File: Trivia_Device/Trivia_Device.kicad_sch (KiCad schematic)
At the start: 5 parts, among them J1 Conn_01x16, J2 Conn_01x16, J3 Conn_01x16, J4 Conn_01x16, U1 BC40C

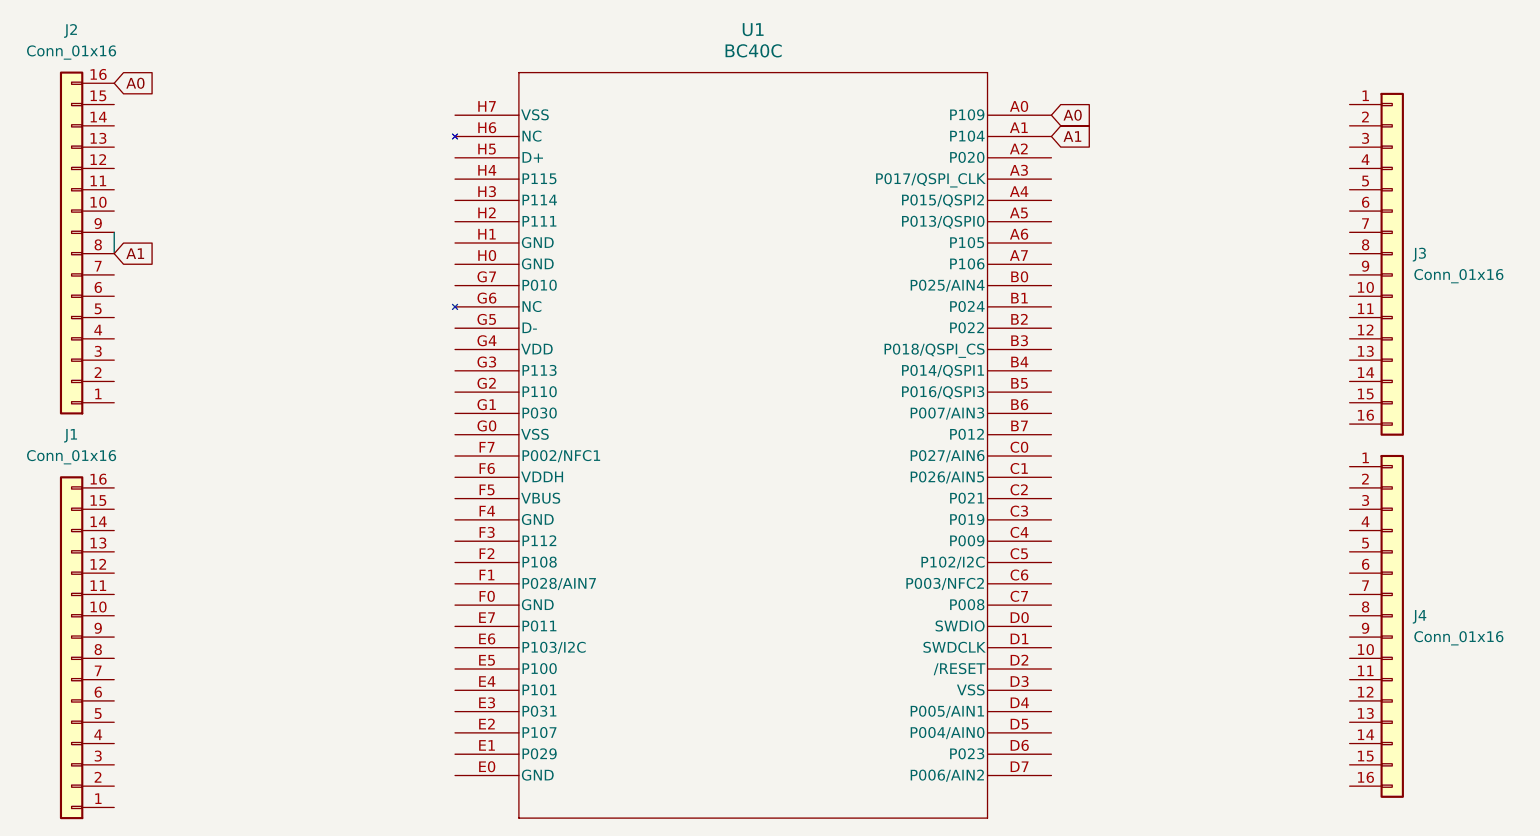
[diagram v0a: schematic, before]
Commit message: working on PCB for processor board
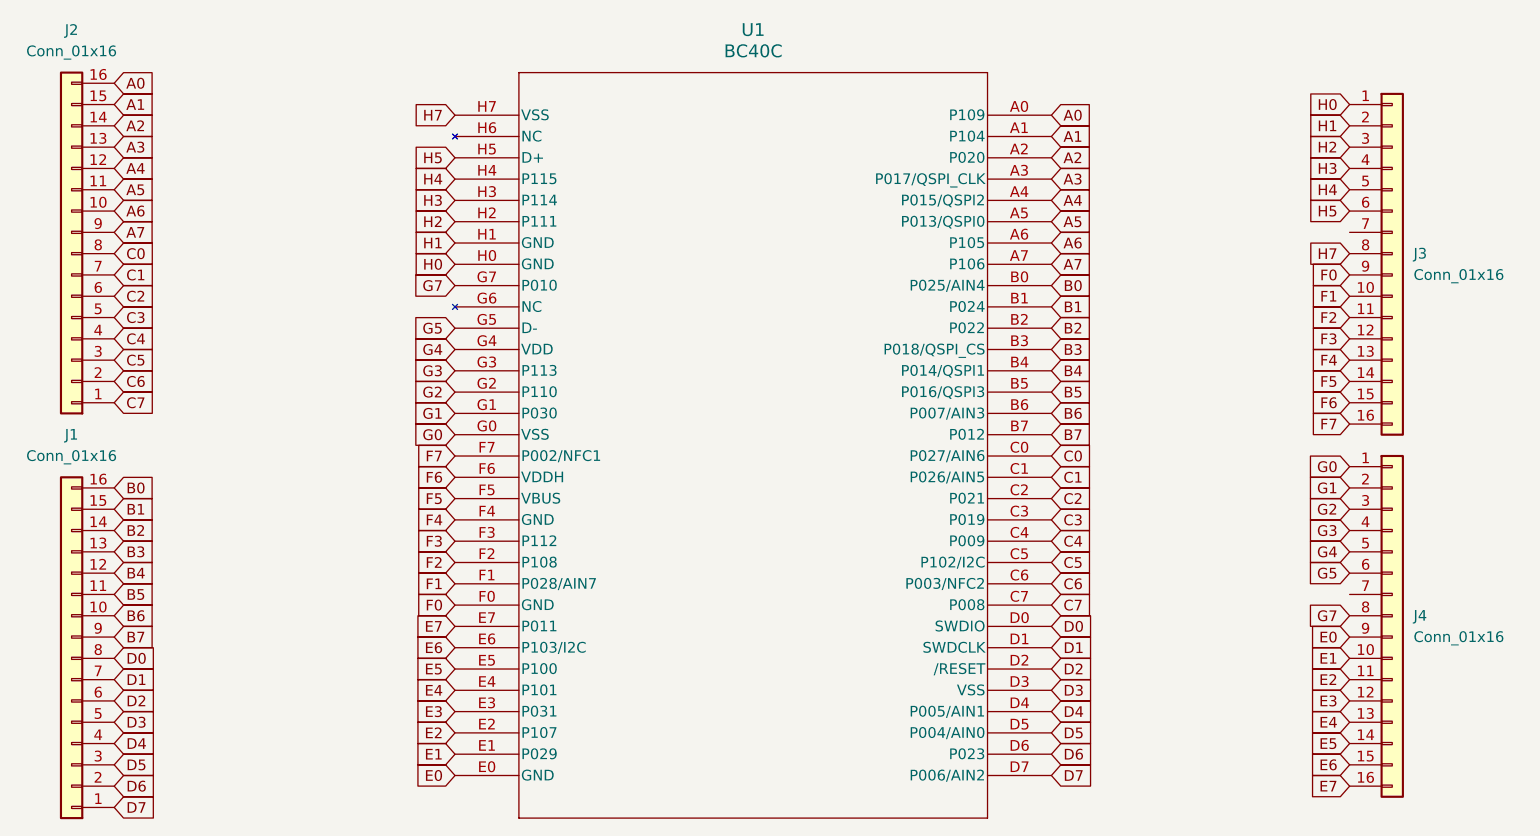
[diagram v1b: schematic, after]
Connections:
- net A1: now also J2.15 (Pin_15); no longer J2.8 (Pin_8), J2.9 (Pin_9)
- net G0: now reaches J4.1 (Pin_1)
- net G0: now also U1.G0 (VSS)
- net E1: now reaches J4.10 (Pin_10)
- net E1: now also U1.E1 (P029)
- net E2: now reaches J4.11 (Pin_11)
- net E2: now also U1.E2 (P107)
- net E3: now reaches J4.12 (Pin_12)
- net E3: now also U1.E3 (P031)
- net E4: now reaches J4.13 (Pin_13)
- net E4: now also U1.E4 (P101)
- net E5: now reaches J4.14 (Pin_14)
- net E5: now also U1.E5 (P100)
- net E6: now reaches J4.15 (Pin_15)
- net E6: now also U1.E6 (P103/I2C)
- net E7: now reaches J4.16 (Pin_16)
- net E7: now also U1.E7 (P011)
- net G1: now reaches J4.2 (Pin_2)
- net G1: now also U1.G1 (P030)
- net G2: now reaches J4.3 (Pin_3)
- net G2: now also U1.G2 (P110)
- net G3: now reaches J4.4 (Pin_4)
- net G3: now also U1.G3 (P113)
- net G4: now reaches J4.5 (Pin_5)
- net G4: now also U1.G4 (VDD)
- net G5: now reaches J4.6 (Pin_6)
- net G5: now also U1.G5 (D-)
- net G7: now reaches J4.8 (Pin_8)
- net G7: now also U1.G7 (P010)
- net E0: now reaches J4.9 (Pin_9)
- net E0: now also U1.E0 (GND)
- net A2: now reaches U1.A2 (P020)
- net A2: now also J2.14 (Pin_14)
- net A3: now reaches U1.A3 (P017/QSPI_CLK)
- net A3: now also J2.13 (Pin_13)
- net A4: now reaches U1.A4 (P015/QSPI2)
- net A4: now also J2.12 (Pin_12)
- net A5: now reaches U1.A5 (P013/QSPI0)
- net A5: now also J2.11 (Pin_11)
- net A6: now reaches U1.A6 (P105)
- net A6: now also J2.10 (Pin_10)
- net A7: now reaches U1.A7 (P106)
- net A7: now also J2.9 (Pin_9)
- net B0: now reaches U1.B0 (P025/AIN4)
- net B0: now also J1.16 (Pin_16)
- net B1: now reaches U1.B1 (P024)
- net B1: now also J1.15 (Pin_15)
- net B2: now reaches U1.B2 (P022)
- net B2: now also J1.14 (Pin_14)
- net B3: now reaches U1.B3 (P018/QSPI_CS)
- net B3: now also J1.13 (Pin_13)
- net B4: now reaches U1.B4 (P014/QSPI1)
- net B4: now also J1.12 (Pin_12)
- net B5: now reaches U1.B5 (P016/QSPI3)
- net B5: now also J1.11 (Pin_11)
- net B6: now reaches U1.B6 (P007/AIN3)
- net B6: now also J1.10 (Pin_10)
- net B7: now reaches U1.B7 (P012)
- net B7: now also J1.9 (Pin_9)
- net C0: now reaches U1.C0 (P027/AIN6)
- net C0: now also J2.8 (Pin_8)
- net C1: now reaches U1.C1 (P026/AIN5)
- net C1: now also J2.7 (Pin_7)
- net C2: now reaches U1.C2 (P021)
- net C2: now also J2.6 (Pin_6)
- net C3: now reaches U1.C3 (P019)
- net C3: now also J2.5 (Pin_5)
- net C4: now reaches U1.C4 (P009)
- net C4: now also J2.4 (Pin_4)
- net C5: now reaches U1.C5 (P102/I2C)
- net C5: now also J2.3 (Pin_3)
- net C6: now reaches U1.C6 (P003/NFC2)
- net C6: now also J2.2 (Pin_2)
- net C7: now reaches U1.C7 (P008)
- net C7: now also J2.1 (Pin_1)
- net D0: now reaches U1.D0 (SWDIO)
- net D0: now also J1.8 (Pin_8)
- net D1: now reaches U1.D1 (SWDCLK)
- net D1: now also J1.7 (Pin_7)
- net D2: now reaches U1.D2 (/RESET)
- net D2: now also J1.6 (Pin_6)
- net D3: now reaches U1.D3 (VSS)
- net D3: now also J1.5 (Pin_5)
- net D4: now reaches U1.D4 (P005/AIN1)
- net D4: now also J1.4 (Pin_4)
- net D5: now reaches U1.D5 (P004/AIN0)
- net D5: now also J1.3 (Pin_3)
- net D6: now reaches U1.D6 (P023)
- net D6: now also J1.2 (Pin_2)
- net D7: now reaches U1.D7 (P006/AIN2)
- net D7: now also J1.1 (Pin_1)
- net F0: now reaches U1.F0 (GND)
- net F0: now also J3.9 (Pin_9)
- net F1: now reaches U1.F1 (P028/AIN7)
- net F1: now also J3.10 (Pin_10)
- net F2: now reaches U1.F2 (P108)
- net F2: now also J3.11 (Pin_11)
- net F3: now reaches U1.F3 (P112)
- net F3: now also J3.12 (Pin_12)
- net F4: now reaches U1.F4 (GND)
- net F4: now also J3.13 (Pin_13)
- net F5: now reaches U1.F5 (VBUS)
- net F5: now also J3.14 (Pin_14)
- net F6: now reaches U1.F6 (VDDH)
- net F6: now also J3.15 (Pin_15)
- net F7: now reaches U1.F7 (P002/NFC1)
- net F7: now also J3.16 (Pin_16)
- net H0: now reaches U1.H0 (GND)
- net H0: now also J3.1 (Pin_1)
- net H1: now reaches U1.H1 (GND)
- net H1: now also J3.2 (Pin_2)
- net H2: now reaches U1.H2 (P111)
- net H2: now also J3.3 (Pin_3)
- net H3: now reaches U1.H3 (P114)
- net H3: now also J3.4 (Pin_4)
- net H4: now reaches U1.H4 (P115)
- net H4: now also J3.5 (Pin_5)
- net H5: now reaches U1.H5 (D+)
- net H5: now also J3.6 (Pin_6)
- net H7: now reaches U1.H7 (VSS)
- net H7: now also J3.8 (Pin_8)
